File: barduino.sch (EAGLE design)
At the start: 21 parts, among them Q2 16MHz, X1 MINI-USB-UX60A-MB-5ST

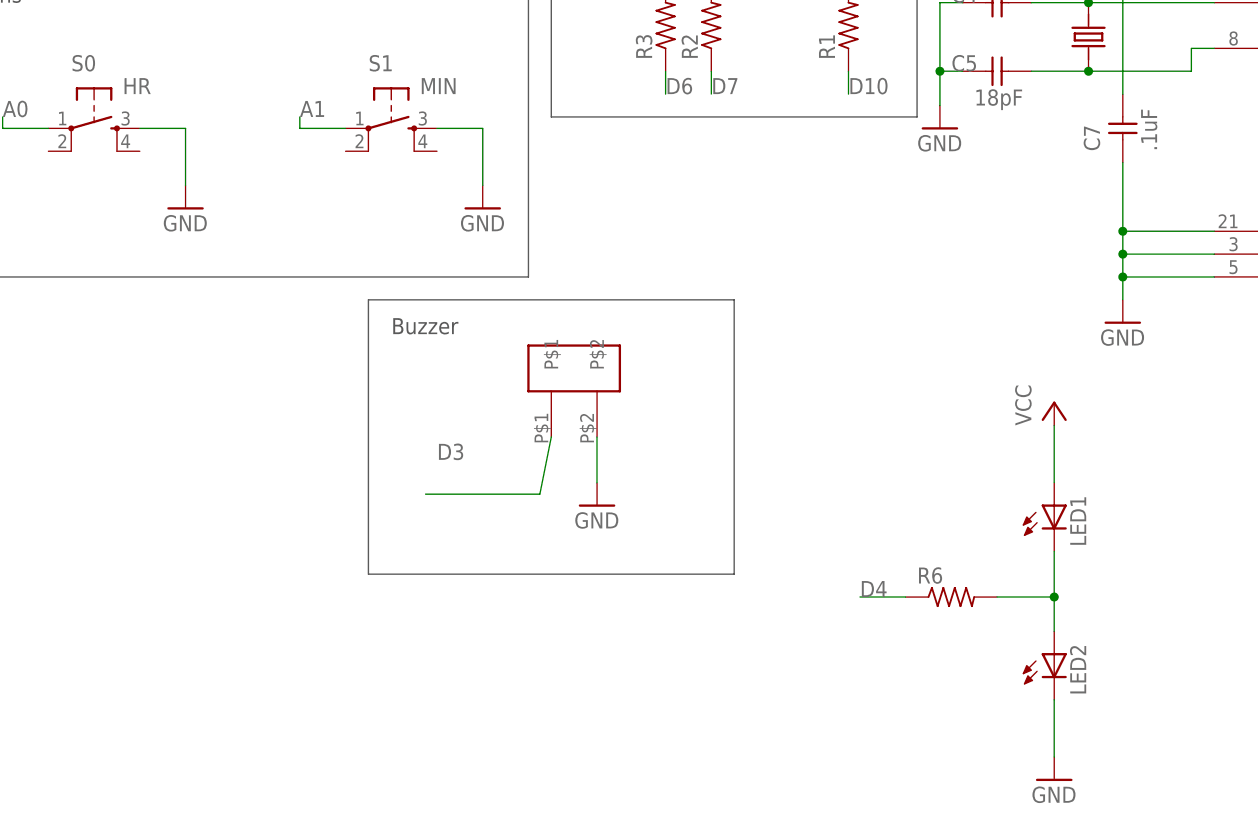
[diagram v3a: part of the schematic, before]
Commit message: add border around schematic and values
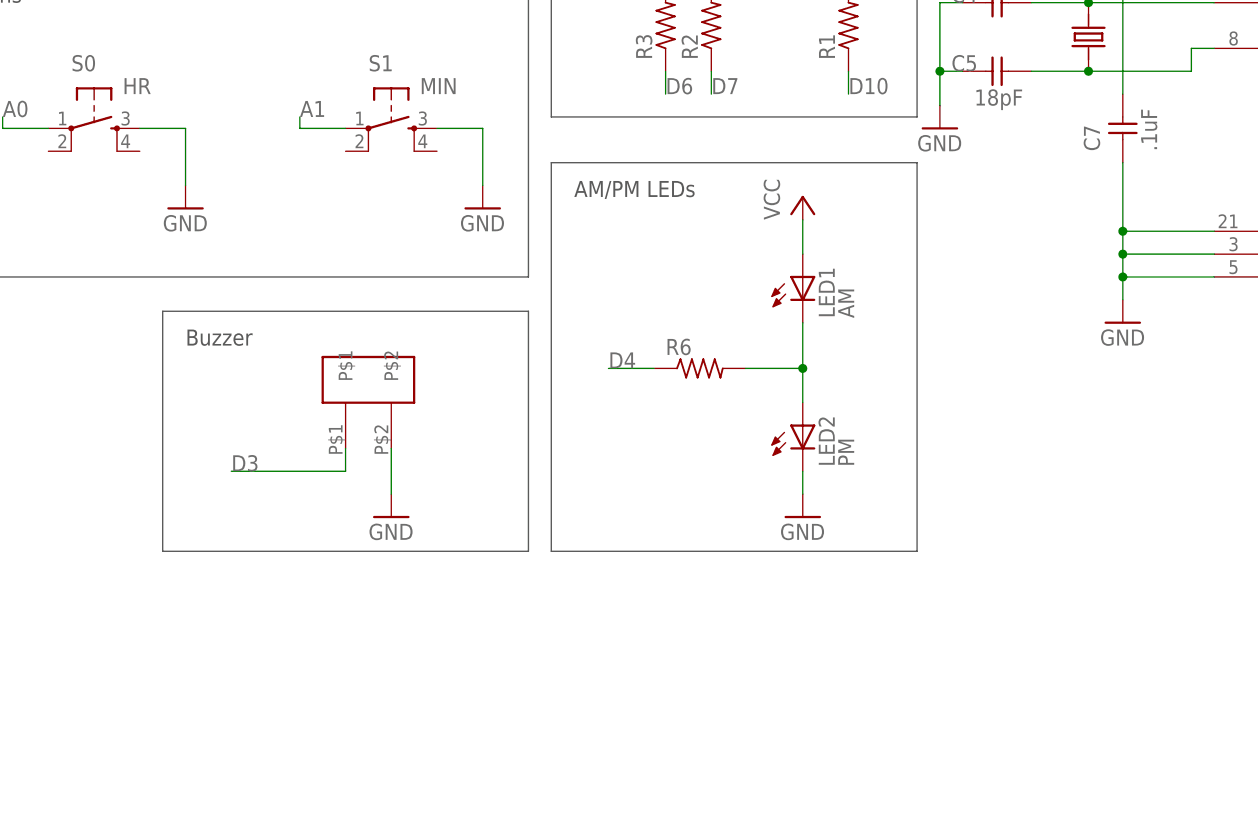
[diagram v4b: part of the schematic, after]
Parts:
- LED1: value (none) -> AM
- LED2: value (none) -> PM
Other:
- note added: "AM/PM LEDs"
- moved on the sheet: LED1, LED2, R6
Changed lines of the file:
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@@
 <part name="R3" library="resistor" deviceset="R-US_" device="R1206"/>
 <part name="R4" library="resistor" deviceset="R-US_" device="R1206"/>
-<part name="LED1" library="led" deviceset="LED" device="CHIPLED_1206"/>
-<part name="LED2" library="led" deviceset="LED" device="CHIPLED_1206"/>
+<part name="LED1" library="led" deviceset="LED" device="CHIPLED_1206" value="AM"/>
+<part name="LED2" library="led" deviceset="LED" device="CHIPLED_1206" value="PM"/>
 <part name="P+5" library="supply1" deviceset="VCC" device=""/>
 <part name="GND8" library="supply1" library_urn="urn:adsk.eagle:library:371" deviceset="GND" device=""/>
@@
 <text x="76.2" y="15.24" size="2.54" layer="91">Arduino compatible / Fabian Based</text>
 <text x="76.2" y="10.16" size="2.54" layer="91">FabLab Approved</text>
-<text x="-22.86" y="34.29" size="1.778" layer="97">Buzzer</text>
+<text x="-45.72" y="33.02" size="1.778" layer="97">Buzzer</text>
 <text x="-2.54" y="129.54" size="1.778" layer="97">DISPLAY</text>
 <wire x1="-5.08" y1="132.08" x2="-5.08" y2="58.42" width="0.1524" layer="97"/>
@@
 <wire x1="-7.62" y1="40.64" x2="-73.66" y2="40.64" width="0.1524" layer="97"/>
 <wire x1="-73.66" y1="40.64" x2="-73.66" y2="73.66" width="0.1524" layer="97"/>
-<wire x1="-25.4" y1="38.1" x2="-25.4" y2="7.62" width="0.1524" layer="97"/>
-<wire x1="-25.4" y1="7.62" x2="15.24" y2="7.62" width="0.1524" layer="97"/>
-<wire x1="15.24" y1="7.62" x2="15.24" y2="38.1" width="0.1524" layer="97"/>
-<wire x1="15.24" y1="38.1" x2="-25.4" y2="38.1" width="0.1524" layer="97"/>
+<wire x1="-48.26" y1="36.83" x2="-48.26" y2="10.16" width="0.1524" layer="97"/>
+<wire x1="-48.26" y1="10.16" x2="-7.62" y2="10.16" width="0.1524" layer="97"/>
+<wire x1="-7.62" y1="10.16" x2="-7.62" y2="36.83" width="0.1524" layer="97"/>
+<wire x1="-7.62" y1="36.83" x2="-48.26" y2="36.83" width="0.1524" layer="97"/>
 <wire x1="68.58" y1="137.16" x2="68.58" y2="104.14" width="0.1524" layer="97"/>
 <wire x1="68.58" y1="104.14" x2="116.84" y2="104.14" width="0.1524" layer="97"/>
 <wire x1="116.84" y1="104.14" x2="116.84" y2="137.16" width="0.1524" layer="97"/>
 <wire x1="116.84" y1="137.16" x2="68.58" y2="137.16" width="0.1524" layer="97"/>
-<text x="29.21" y="5.08" size="1.778" layer="95">D4</text>
+<text x="1.27" y="30.48" size="1.778" layer="95">D4</text>
+<text x="-2.54" y="49.53" size="1.778" layer="97">AM/PM LEDs</text>
+<wire x1="-5.08" y1="53.34" x2="-5.08" y2="10.16" width="0.1524" layer="97"/>
+<wire x1="-5.08" y1="10.16" x2="35.56" y2="10.16" width="0.1524" layer="97"/>
+<wire x1="35.56" y1="10.16" x2="35.56" y2="53.34" width="0.1524" layer="97"/>
+<wire x1="35.56" y1="53.34" x2="-5.08" y2="53.34" width="0.1524" layer="97"/>
 </plain>
 <instances>
@@
 <instance part="U$1" gate="G$1" x="91.44" y="71.12"/>
 <instance part="ICSP" gate="A" x="88.9" y="116.84"/>
-<instance part="GND2" gate="1" x="0" y="15.24"/>
+<instance part="GND2" gate="1" x="-22.86" y="13.97"/>
 <instance part="GND1" gate="1" x="-13.97" y="85.09"/>
 <instance part="P+1" gate="VCC" x="64.77" y="121.92"/>
@@
 <instance part="GND3" gate="1" x="58.42" y="35.56"/>
 <instance part="X1" gate="G$1" x="-30.48" y="99.06" rot="MR0"/>
-<instance part="U$4" gate="G$1" x="-2.54" y="30.48"/>
+<instance part="U$4" gate="G$1" x="-25.4" y="29.21"/>
 <instance part="R1" gate="G$1" x="27.94" y="68.58" rot="R90"/>
 <instance part="R2" gate="G$1" x="12.7" y="68.58" rot="R90"/>
 <instance part="R3" gate="G$1" x="7.62" y="68.58" rot="R90"/>
 <instance part="R4" gate="G$1" x="2.54" y="101.6" rot="R90"/>
-<instance part="LED1" gate="G$1" x="50.8" y="15.24"/>
-<instance part="LED2" gate="G$1" x="50.8" y="-1.27"/>
-<instance part="P+5" gate="VCC" x="50.8" y="26.67"/>
-<instance part="GND8" gate="1" x="50.8" y="-15.24"/>
-<instance part="R6" gate="G$1" x="39.37" y="5.08"/>
+<instance part="LED1" gate="G$1" x="22.86" y="40.64"/>
+<instance part="LED2" gate="G$1" x="22.86" y="24.13"/>
+<instance part="P+5" gate="VCC" x="22.86" y="49.53"/>
+<instance part="GND8" gate="1" x="22.86" y="13.97"/>
+<instance part="R6" gate="G$1" x="11.43" y="30.48"/>
 </instances>
 <busses>
@@
 </segment>
 <segment>
-<wire x1="50.8" y1="24.13" x2="50.8" y2="17.78" width="0.1524" layer="91"/>
+<wire x1="22.86" y1="46.99" x2="22.86" y2="43.18" width="0.1524" layer="91"/>
 <pinref part="P+5" gate="VCC" pin="VCC"/>
 <pinref part="LED1" gate="G$1" pin="A"/>
@@
 <pinref part="GND2" gate="1" pin="GND"/>
 <pinref part="U$4" gate="G$1" pin="P$2"/>
-<wire x1="0" y1="17.78" x2="0" y2="22.86" width="0.1524" layer="91"/>
+<wire x1="-22.86" y1="16.51" x2="-22.86" y2="21.59" width="0.1524" layer="91"/>
 </segment>
 <segment>
 <pinref part="GND8" gate="1" pin="GND"/>
-<wire x1="50.8" y1="-12.7" x2="50.8" y2="-6.35" width="0.1524" layer="91"/>
+<wire x1="22.86" y1="16.51" x2="22.86" y2="19.05" width="0.1524" layer="91"/>
 <pinref part="LED2" gate="G$1" pin="C"/>
 </segment>
@@
 <segment>
 <pinref part="U$4" gate="G$1" pin="P$1"/>
-<wire x1="-5.08" y1="22.86" x2="-6.35" y2="16.51" width="0.1524" layer="91"/>
-<wire x1="-6.35" y1="16.51" x2="-19.05" y2="16.51" width="0.1524" layer="91"/>
-<label x="-17.78" y="20.32" size="1.778" layer="95"/>
+<wire x1="-27.94" y1="21.59" x2="-27.94" y2="19.05" width="0.1524" layer="91"/>
+<wire x1="-27.94" y1="19.05" x2="-40.64" y2="19.05" width="0.1524" layer="91"/>
+<label x="-40.64" y="19.05" size="1.778" layer="95"/>
 </segment>
 </net>
@@
 <segment>
 <pinref part="R6" gate="G$1" pin="1"/>
-<wire x1="34.29" y1="5.08" x2="29.21" y2="5.08" width="0.1524" layer="91"/>
+<wire x1="6.35" y1="30.48" x2="1.27" y2="30.48" width="0.1524" layer="91"/>
 </segment>
 </net>
@@
 <segment>
 <pinref part="LED2" gate="G$1" pin="A"/>
-<wire x1="50.8" y1="1.27" x2="50.8" y2="5.08" width="0.1524" layer="91"/>
+<wire x1="22.86" y1="26.67" x2="22.86" y2="30.48" width="0.1524" layer="91"/>
 <pinref part="LED1" gate="G$1" pin="C"/>
 <pinref part="R6" gate="G$1" pin="2"/>
-<wire x1="50.8" y1="5.08" x2="50.8" y2="10.16" width="0.1524" layer="91"/>
-<wire x1="44.45" y1="5.08" x2="50.8" y2="5.08" width="0.1524" layer="91"/>
-<junction x="50.8" y="5.08"/>
-</segment>
-</net>
+<wire x1="22.86" y1="30.48" x2="22.86" y2="35.56" width="0.1524" layer="91"/>
+<wire x1="16.51" y1="30.48" x2="22.86" y2="30.48" width="0.1524" layer="91"/>
+<junction x="22.86" y="30.48"/>
+</segment>
+</net>

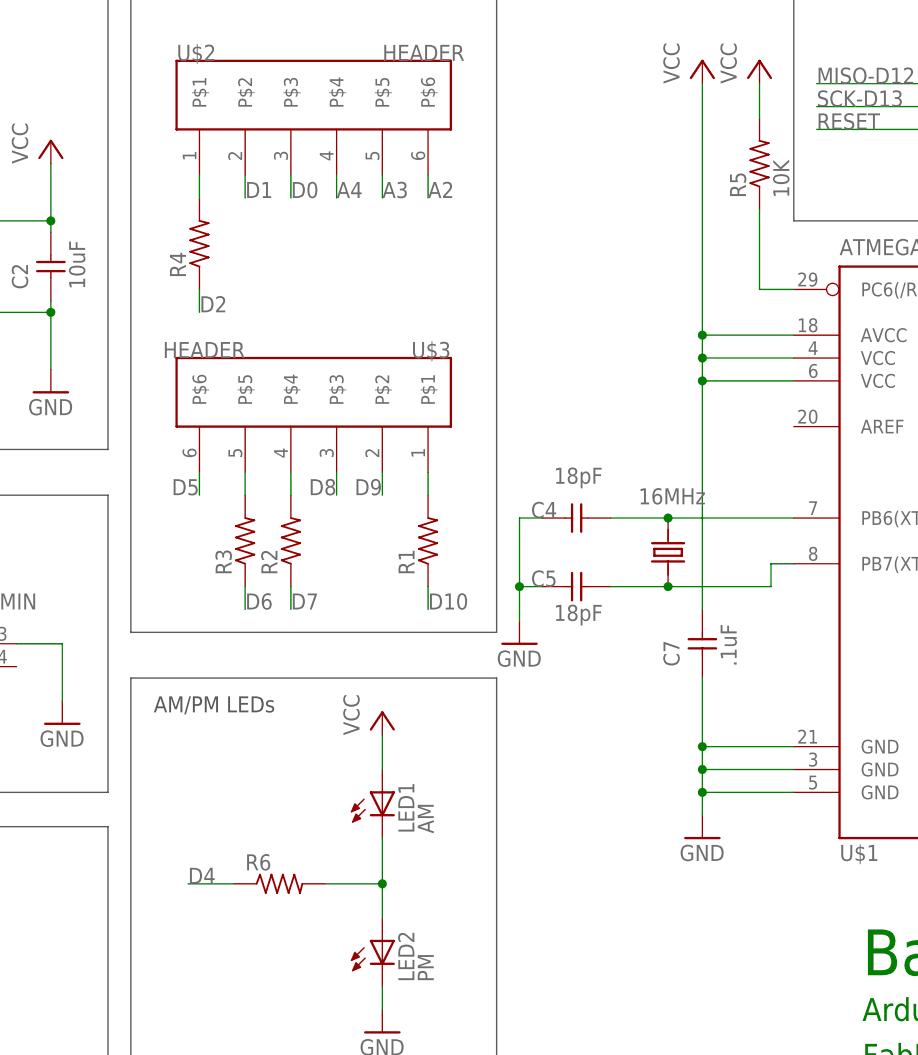
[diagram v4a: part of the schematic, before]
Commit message: Add resistors to segments, not digits
1. Renamed reset and AM/PM LED R's
2. Fixed error on LED net
3. Moved/added resistors to all 8 segments
4. Updated eagle
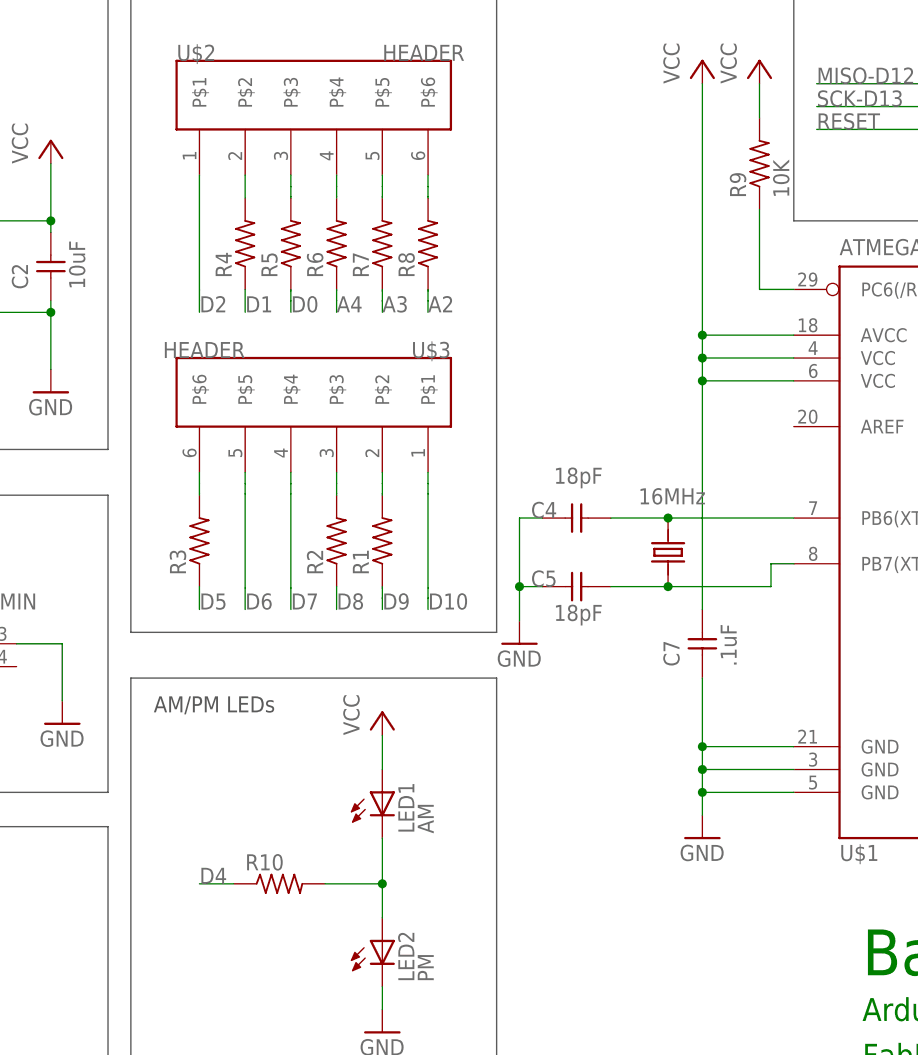
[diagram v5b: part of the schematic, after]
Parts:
- added R10, R7, R8: (no value), resistor:R-US_R1206
- added R9: 10K, ng:RESISTOR1206
- R5: value 10K -> (none); device ng:RESISTOR1206 -> resistor:R-US_R1206
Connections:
- removed net N$1: R1.2, U$3.P$1
- removed net N$2: R2.2, U$3.P$4
- removed net N$3: R3.2, U$3.P$5
- new net N$10: R5.2, U$2.P$3
- new net N$22: R4.2, U$2.P$2
- new net N$23: R6.2, U$2.P$4
- new net N$29: R2.2, U$3.P$3
- new net N$33: R1.2, U$3.P$2
- new net N$8: R8.2, U$2.P$6
- new net N$9: R7.2, U$2.P$5
- net A2: now also R8.1; no longer U$2.P$6
- net A3: now also R7.1; no longer U$2.P$5
- net A4: now also R6.1; no longer U$2.P$4
- net D0: now also R5.1; no longer U$2.P$3
- net D1: now also R4.1; no longer U$2.P$2
- net D10: now also U$3.P$1; no longer R1.1
- net D2: now also U$2.P$1; no longer R4.1
- net D4: now also R10.1; no longer R6.1
- net D5: now also R3.1; no longer U$3.P$6
- net D6: now also U$3.P$5; no longer R3.1
- net D7: now also U$3.P$4; no longer R2.1
- net D8: now also R2.1; no longer U$3.P$3
- net D9: now also R1.1; no longer U$3.P$2
- net N$4: now also R3.2, U$3.P$6; no longer R4.2, U$2.P$1
- net N$5: now also R10.2; no longer R6.2
- net RESET: now also R9.1; no longer R5.1
- net VCC: now also R9.2; no longer R5.2
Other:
- note removed: "D4"
- moved on the sheet: R1, R2, R3, R4, R5, R6

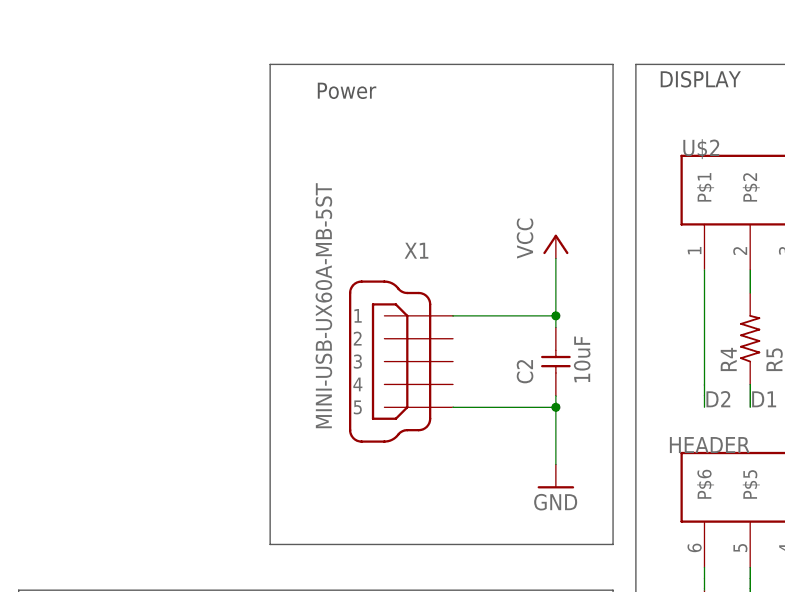
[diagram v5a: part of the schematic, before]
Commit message: Put new USB power connector on sch/brd
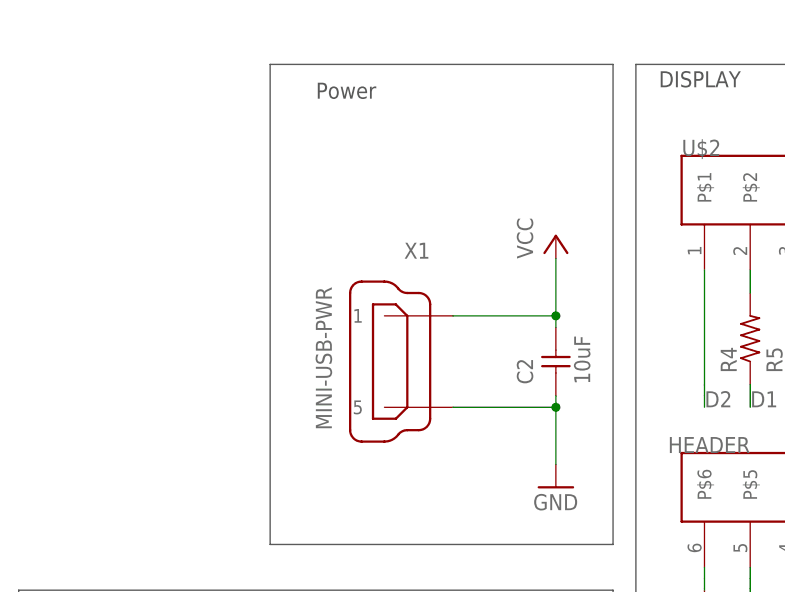
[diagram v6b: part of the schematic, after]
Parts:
- X1: value MINI-USB-UX60A-MB-5ST -> MINI-USB-PWR; device con-hirose:MINI-USB-UX60A-MB-5ST -> 4-Digit-Clock:MINI-USB-PWR
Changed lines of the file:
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@@
 <part name="GND7" library="supply1" library_urn="urn:adsk.eagle:library:371" deviceset="GND" device=""/>
 <part name="GND3" library="supply1" library_urn="urn:adsk.eagle:library:371" deviceset="GND" device=""/>
-<part name="X1" library="con-hirose" deviceset="MINI-USB-" device="UX60A-MB-5ST"/>
 <part name="U$4" library="4-Digit-Clock" deviceset="BUZZER" device=""/>
 <part name="R1" library="resistor" deviceset="R-US_" device="R1206"/>
@@
 <part name="R7" library="resistor" deviceset="R-US_" device="R1206"/>
 <part name="R8" library="resistor" deviceset="R-US_" device="R1206"/>
+<part name="X1" library="4-Digit-Clock" deviceset="MINI-USB-PWR" device=""/>
 </parts>
 <sheets>
@@
 <instance part="GND7" gate="1" x="-12.7" y="48.26"/>
 <instance part="GND3" gate="1" x="58.42" y="35.56"/>
-<instance part="X1" gate="G$1" x="-30.48" y="99.06" rot="MR0"/>
 <instance part="U$4" gate="G$1" x="-25.4" y="29.21"/>
 <instance part="R1" gate="G$1" x="22.86" y="68.58" rot="R90"/>
@@
 <instance part="R7" gate="G$1" x="22.86" y="101.6" rot="R90"/>
 <instance part="R8" gate="G$1" x="27.94" y="101.6" rot="R90"/>
+<instance part="X1" gate="G$1" x="-30.48" y="99.06" rot="MR0"/>
 </instances>
 <busses>
@@
 with this version.
 </note>
+<note version="8.3" severity="warning">
+Since Version 8.3, EAGLE supports URNs for individual library
+assets (packages, symbols, and devices). The URNs of those assets
+will not be understood (or retained) with this version.
+</note>
 </compatibility>

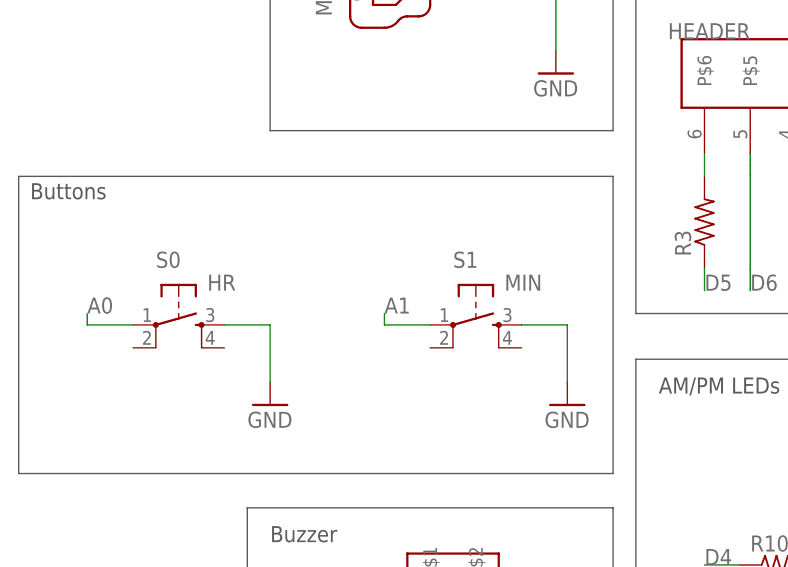
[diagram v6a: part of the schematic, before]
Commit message: Buttons don't have a value
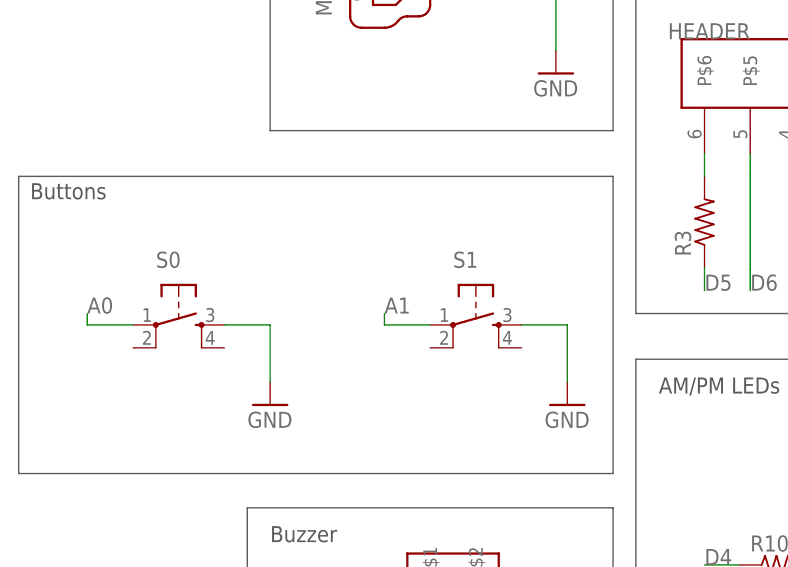
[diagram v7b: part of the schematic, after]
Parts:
- S0: value HR -> (none)
- S1: value MIN -> (none)
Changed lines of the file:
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@@
 <part name="R9" library="ng" deviceset="RESISTOR" device="1206" value="10K"/>
 <part name="P+2" library="supply1" deviceset="VCC" device=""/>
-<part name="S0" library="ng" deviceset="6MM_SWITCH" device="6MM_SWITCH" value="HR"/>
+<part name="S0" library="ng" deviceset="6MM_SWITCH" device="6MM_SWITCH"/>
 <part name="C2" library="ng" deviceset="UNPOLARIZED_CAPACITOR" device="1206" value="10uF"/>
 <part name="C7" library="ng" deviceset="UNPOLARIZED_CAPACITOR" device="1206" value=".1uF"/>
@@
 <part name="GND1" library="supply1" library_urn="urn:adsk.eagle:library:371" deviceset="GND" device=""/>
 <part name="P+1" library="supply1" library_urn="urn:adsk.eagle:library:371" deviceset="VCC" device=""/>
-<part name="S1" library="ng" deviceset="6MM_SWITCH" device="6MM_SWITCH" value="MIN"/>
+<part name="S1" library="ng" deviceset="6MM_SWITCH" device="6MM_SWITCH"/>
 <part name="P+4" library="supply1" library_urn="urn:adsk.eagle:library:371" deviceset="VCC" device=""/>
 <part name="GND5" library="supply1" library_urn="urn:adsk.eagle:library:371" deviceset="GND" device=""/>
